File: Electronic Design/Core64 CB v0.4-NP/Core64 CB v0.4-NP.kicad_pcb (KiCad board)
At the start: 2 copper layers, 85 x 85 mm, 16 parts, among them J1 TSM-116-03-T-SV‎, J2 TSM-116-03-T-SV‎, U1 SI7210-B-01, U2 SI7210-B-02, U3 SI7210-B-03, U4 SI7210-B-04, U5 LTR-329ALS-01, X1 SAO_conn_SFH11-NBPC-D03-ST-BK

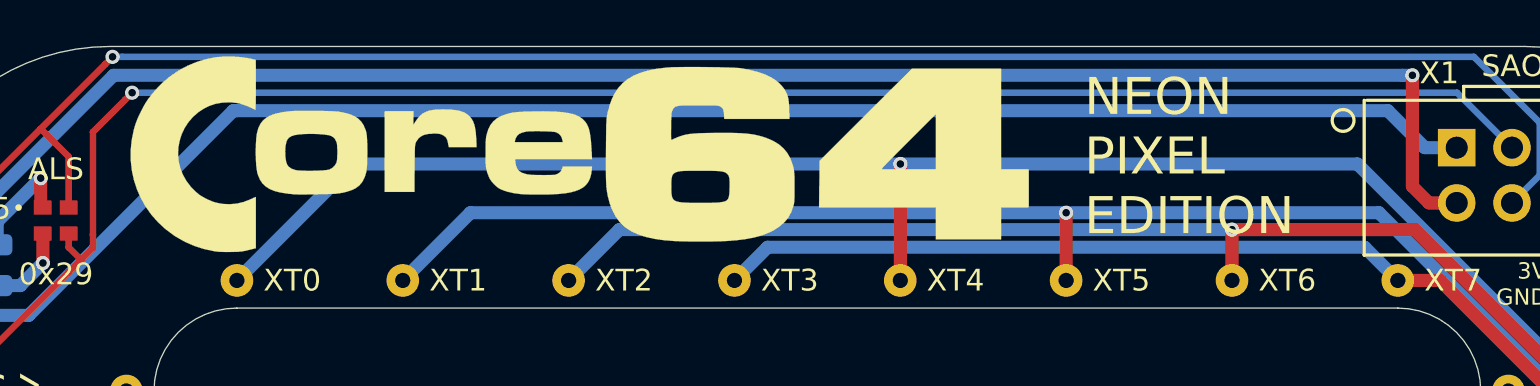
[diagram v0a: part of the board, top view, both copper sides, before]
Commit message: Tweak LB V0.4-NP Core64 logo position
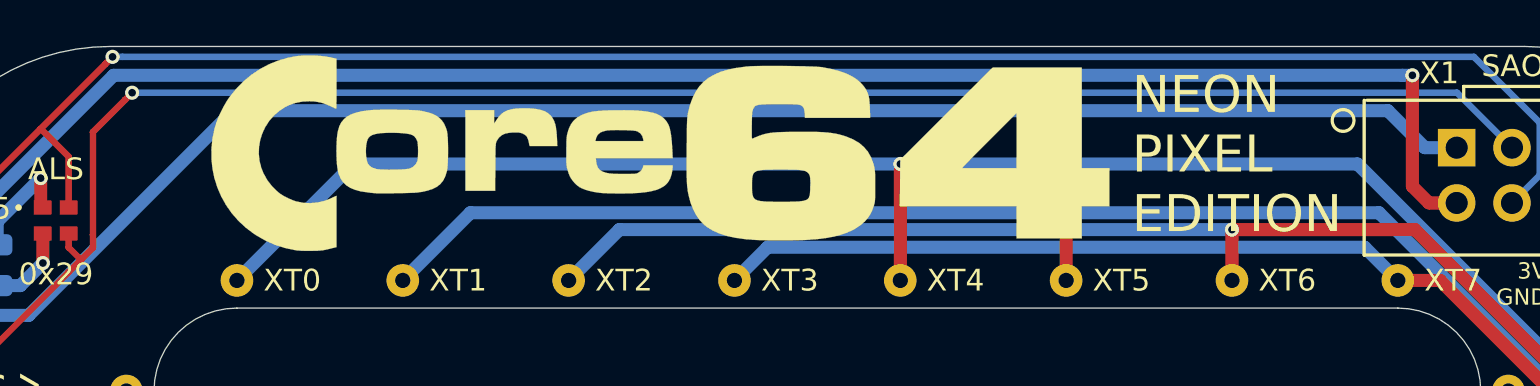
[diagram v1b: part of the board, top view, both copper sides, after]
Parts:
- moved L1 3.71 mm to (-5.33, -37.6)
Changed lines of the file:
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@@
   )
   (module Core_Memory_8x8_Array:Core64_Logo_9mm_tall (layer F.Cu)
-    (at -9.035 -37.57)
+    (at -5.3266 -37.6208)
     (fp_text reference L1 (at 0 -27) (layer F.SilkS) hide
       (effects (font (size 1.524 1.524) (thickness 0.3)))
@@
   (gr_line (start 30.48 -26.67) (end 30.48 26.67) (layer Edge.Cuts) (width 0.05))
   (gr_line (start -26.67 -30.48) (end 26.67 -30.48) (layer Edge.Cuts) (width 0.05))
-  (gr_text "NEON\nPIXEL\nEDITION" (at 12.265 -37.45) (layer F.SilkS)
+  (gr_text "NEON\nPIXEL\nEDITION" (at 14.4526 -37.5412) (layer F.SilkS)
     (effects (font (size 1.7 1.7) (thickness 0.4)) (justify left))
   )

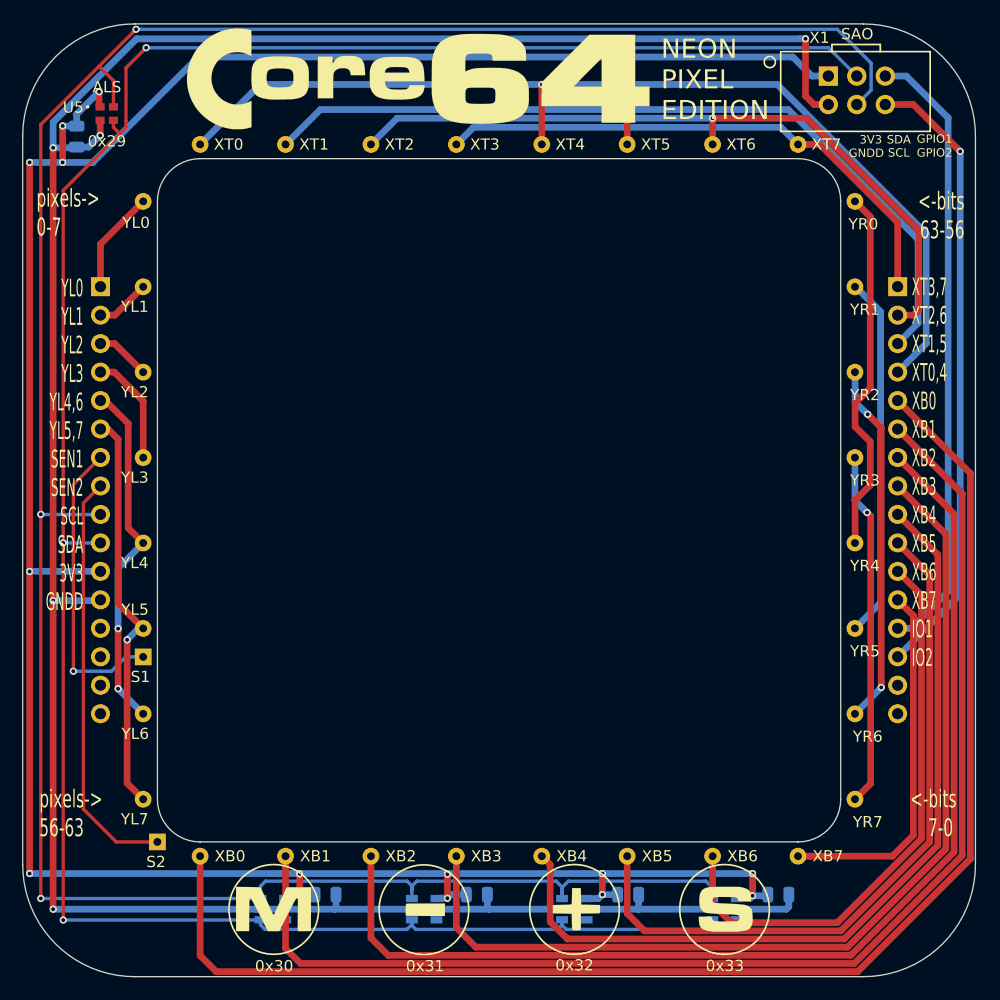
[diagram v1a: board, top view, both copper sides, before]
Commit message: Complete layout and create NP Gerbers for quote
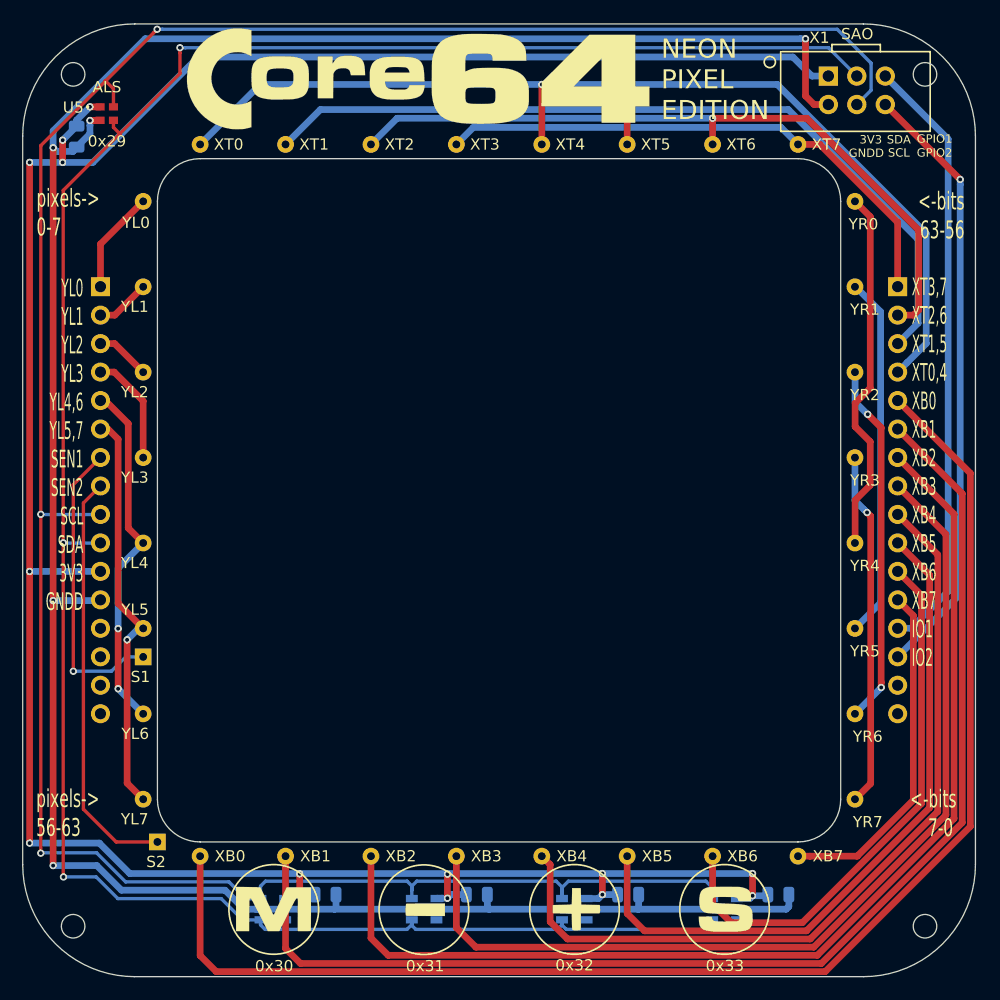
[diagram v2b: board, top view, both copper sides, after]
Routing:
- net I2C_CLOCK: track 228.4 -> 223.4 mm
- net 3V3_800mA: track 239.4 -> 234.9 mm
- net I2C_DATA: track 212.5 -> 208.4 mm
- net GNDD: track 228.8 -> 226.3 mm
- net XB7: track 32.6 -> 30.8 mm
- net XB6: track 51.4 -> 49.6 mm
- net XB5: track 63.9 -> 62.1 mm
- net XB4: track 75.8 -> 74.1 mm
- net XB3: track 88.6 -> 86.8 mm
- net XB2: track 101.1 -> 99.3 mm
- net XB1: track 113.7 -> 111.9 mm
- net XB0: track 125.9 -> 124.2 mm
- net SAO_GPIO2: track 55.8 -> 54.4 mm
- net SAO_GPIO1: track 55.3 -> 54.2 mm
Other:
- outline, holes or cut-outs redrawn
- board text added: "CORE BOARD V0.4-NP NEON PIXELS EDITION 2020-11-24 ANDY GEPPERT"
- board text removed: "CORE BOARD V0.4-NP NEON PIXELS EDITION 2020-11-23 ANDY GEPPERT"

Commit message: Update Simple Add Ons #2 on all schematics PCBs
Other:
- board text added: "J1"
- board text added: "J2"
- board text added: "NEON PIXELS BY PIERRE MUTH PIERREMUTH.WORDPRESS.COM"
- board text added: "SAO#2"
- board text added: "X1"
- board text removed: "BY PIERRE MUTH PIERREMUTH.WORDPRESS.COM"
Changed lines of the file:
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@@
   (general
     (thickness 1.6)
-    (drawings 55)
+    (drawings 59)
     (tracks 366)
     (zones 0)
@@
     (descr "Through hole straight IDC box header, 2x03, 2.54mm pitch, double rows")
     (tags "Through hole IDC box header THT 2x03 2.54mm double row")
-    (fp_text reference X1 (at -3.28 -4.675) (layer F.SilkS)
+    (fp_text reference X1 (at -3.24 -4.55) (layer F.SilkS)
       (effects (font (size 1 1) (thickness 0.15)))
     )
@@
       (effects (font (size 1 1) (thickness 0.15)))
     )
-    (fp_text user SAO (at 0.1 -5) (layer F.SilkS)
+    (fp_text user SAO#2 (at 0.1 -5) (layer F.SilkS)
       (effects (font (size 1 1) (thickness 0.15)))
     )
@@
       (effects (font (size 0.75 0.75) (thickness 0.15)) (justify mirror))
     )
-    (fp_text user GPIO2 (at 3.2 3.048) (layer B.SilkS)
+    (fp_text user GPIO2 (at 3.4 3.048) (layer B.SilkS)
       (effects (font (size 0.75 0.75) (thickness 0.15)) (justify mirror))
     )
-    (fp_text user SCL (at 0 3.048) (layer B.SilkS)
+    (fp_text user SCL (at 0.2 3.048) (layer B.SilkS)
       (effects (font (size 0.75 0.75) (thickness 0.15)) (justify mirror))
     )
@@
       (effects (font (size 0.75 0.75) (thickness 0.15)) (justify mirror))
     )
-    (fp_text user GNDD (at -3 3.048) (layer B.SilkS)
+    (fp_text user GNDD (at -2.8 3.048) (layer B.SilkS)
       (effects (font (size 0.75 0.75) (thickness 0.15)) (justify mirror))
     )
@@
     )
   )
+  (gr_text SAO#2 (at 38.415 -35.45) (layer B.SilkS)
+    (effects (font (size 1 1) (thickness 0.15)) (justify mirror))
+  )
+  (gr_text J2 (at 35.615 -21.35) (layer F.SilkS)
+    (effects (font (size 1 1) (thickness 0.16)))
+  )
+  (gr_text J1 (at -35.485 -21.35) (layer F.SilkS)
+    (effects (font (size 1 1) (thickness 0.16)))
+  )
+  (gr_text X1 (at 27.015 -37.75) (layer B.SilkS)
+    (effects (font (size 1 1) (thickness 0.15)) (justify mirror))
+  )
   (dimension 76 (width 0.15) (layer Dwgs.User)
     (gr_text "76.000 mm" (at 56.915 0 270) (layer Dwgs.User)
@@
   (gr_circle (center -6.7056 36.5252) (end -2.7056 36.5252) (layer F.SilkS) (width 0.15))
   (gr_circle (center -20.1 36.5) (end -16.1 36.5) (layer F.SilkS) (width 0.15))
-  (gr_text "BY PIERRE MUTH\nPIERREMUTH.WORDPRESS.COM" (at -12.573 -34.036) (layer B.SilkS)
+  (gr_text "NEON PIXELS BY PIERRE MUTH\nPIERREMUTH.WORDPRESS.COM" (at -12.585 -34.15) (layer B.SilkS)
     (effects (font (size 1 1) (thickness 0.15)) (justify left mirror))
   )

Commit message: Export Gerbers and order 10, export updated schematic and front/back renders
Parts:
- added ?: , , F.Cu at (16.3, -8.15)
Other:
- board text added: "CORE BOARD V0.4-NP NEON PIXEL EDITION 2020-11-25 ANDY GEPPERT"
- board text removed: "CORE BOARD V0.4-NP NEON PIXELS EDITION 2020-11-24 ANDY GEPPERT"
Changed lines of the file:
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@@
     (tracks 366)
     (zones 0)
-    (modules 16)
+    (modules 17)
     (nets 41)
   )
@@
     (38 B.Mask user)
     (39 F.Mask user)
-    (40 Dwgs.User user)
+    (40 Dwgs.User user hide)
     (41 Cmts.User user hide)
     (42 Eco1.User user hide)
@@
       (drillshape 0)
       (scaleselection 1)
-      (outputdirectory "Core64 CB v0.4-NP Gerbers (2020-11-24)/"))
+      (outputdirectory "Core64 CB v0.4-NP Gerbers (2020-11-25)/"))
   )
   (net 0 "")
@@
     (add_net SENSE2)
   )
+  (module "" (layer F.Cu)
+    (at 16.315 -8.15)
+    (fp_text reference "" (at 31.855 -36.6) (layer F.SilkS)
+      (effects (font (size 1.27 1.27) (thickness 0.15)))
+    )
+    (fp_text value "" (at 31.855 -36.6) (layer F.SilkS)
+      (effects (font (size 1.27 1.27) (thickness 0.15)))
+    )
+    (fp_text user GPIO1 (at 24.2 -24) (layer F.SilkS)
+      (effects (font (size 0.75 0.75) (thickness 0.15)))
+    )
+    (fp_text user GPIO2 (at 24.2 -22.8) (layer F.SilkS)
+      (effects (font (size 0.75 0.75) (thickness 0.15)))
+    )
+    (fp_text user SCL (at 20.9 -22.8) (layer F.SilkS)
+      (effects (font (size 0.75 0.75) (thickness 0.15)))
+    )
+    (fp_text user GNDD (at 17.7 -22.8) (layer F.SilkS)
+      (effects (font (size 0.75 0.75) (thickness 0.15)))
+    )
+    (fp_text user 3V3 (at 17.7 -24) (layer F.SilkS)
+      (effects (font (size 0.75 0.75) (thickness 0.15)))
+    )
+    (fp_text user SDA (at 20.8 -24) (layer F.SilkS)
+      (effects (font (size 0.75 0.75) (thickness 0.15)))
+    )
+  )
   (module badgelife_sao_v169bis:Badgelife-SAOv169-BADGE-2x3 (layer F.Cu)
     (at 31.855 -36.6)
@@
       (effects (font (size 1 1) (thickness 0.15)))
     )
+    (fp_line (start 6.604 3.683) (end 6.604 2.754) (layer F.SilkS) (width 0.15))
+    (fp_line (start 6.604 -2.5) (end 6.604 -3.429) (layer F.SilkS) (width 0.15))
+    (fp_line (start 6.604 -3.429) (end 5.873 -3.429) (layer F.SilkS) (width 0.15))
+    (fp_line (start 6.604 3.683) (end 5.873 3.683) (layer F.SilkS) (width 0.15))
+    (fp_line (start -6.731 3.683) (end -6.731 2.754) (layer F.SilkS) (width 0.15))
+    (fp_line (start -6.731 -3.429) (end -6 -3.429) (layer F.SilkS) (width 0.15))
     (fp_text user SAO#2 (at 0.1 -5) (layer F.SilkS)
       (effects (font (size 1 1) (thickness 0.15)))
-    )
-    (fp_text user 3V3 (at 1.31 4.419) (layer F.SilkS)
-      (effects (font (size 0.75 0.75) (thickness 0.15)))
-    )
-    (fp_text user GNDD (at 0.91 5.619) (layer F.SilkS)
-      (effects (font (size 0.75 0.75) (thickness 0.15)))
-    )
-    (fp_text user SDA (at 3.81 4.419) (layer F.SilkS)
-      (effects (font (size 0.75 0.75) (thickness 0.15)))
-    )
-    (fp_text user SCL (at 3.81 5.592) (layer F.SilkS)
-      (effects (font (size 0.75 0.75) (thickness 0.15)))
-    )
-    (fp_text user GPIO2 (at 6.997 5.592) (layer F.SilkS)
-      (effects (font (size 0.75 0.75) (thickness 0.15)))
-    )
-    (fp_text user GPIO1 (at 6.997 4.35) (layer F.SilkS)
-      (effects (font (size 0.75 0.75) (thickness 0.15)))
     )
     (fp_text user GPIO1 (at 3.2 -2.794) (layer B.SilkS)
       (effects (font (size 0.75 0.75) (thickness 0.15)) (justify mirror))
     )
-    (fp_text user GPIO2 (at 3.4 3.048) (layer B.SilkS)
+    (fp_text user GPIO2 (at 3.2 3.048) (layer B.SilkS)
       (effects (font (size 0.75 0.75) (thickness 0.15)) (justify mirror))
     )
-    (fp_text user SCL (at 0.2 3.048) (layer B.SilkS)
+    (fp_text user SCL (at 0 3.048) (layer B.SilkS)
       (effects (font (size 0.75 0.75) (thickness 0.15)) (justify mirror))
     )
@@
       (effects (font (size 0.75 0.75) (thickness 0.15)) (justify mirror))
     )
-    (fp_text user GNDD (at -2.8 3.048) (layer B.SilkS)
+    (fp_text user GNDD (at -3 3.048) (layer B.SilkS)
       (effects (font (size 0.75 0.75) (thickness 0.15)) (justify mirror))
     )
@@
     (fp_line (start 2.159 -4.064) (end 2.159 -3.43) (layer F.SilkS) (width 0.15))
     (fp_line (start -2.159 -4.064) (end 2.159 -4.064) (layer F.SilkS) (width 0.15))
-    (fp_line (start -6.731 3.683) (end -6.731 -3.429) (layer F.SilkS) (width 0.15))
-    (fp_line (start 6.604 3.683) (end -6.731 3.683) (layer F.SilkS) (width 0.15))
-    (fp_line (start 6.604 -3.429) (end 6.604 3.683) (layer F.SilkS) (width 0.15))
-    (fp_line (start -6.604 -3.429) (end 6.604 -3.429) (layer F.SilkS) (width 0.15))
+    (fp_line (start -6.731 -2.5) (end -6.731 -3.429) (layer F.SilkS) (width 0.15))
+    (fp_line (start -6 3.683) (end -6.731 3.683) (layer F.SilkS) (width 0.15))
     (fp_text user %R (at 0.06 0.02 270) (layer F.Fab)
+      (effects (font (size 1 1) (thickness 0.15)))
+    )
+    (fp_text user SAO#2 (at 0.1 -5) (layer F.SilkS)
       (effects (font (size 1 1) (thickness 0.15)))
     )
@@
     (arrow2b (pts (xy 42.5 -50.549999) (xy 41.373496 -49.963578)))
   )
-  (gr_text "CORE BOARD   V0.4-NP   NEON PIXELS EDITION   2020-11-24   ANDY GEPPERT   " (at -0.685 -41.35) (layer B.SilkS)
+  (gr_text "CORE BOARD   V0.4-NP   NEON PIXEL EDITION   2020-11-25   ANDY GEPPERT   " (at 0 -41.5) (layer B.SilkS)
     (effects (font (size 1 1) (thickness 0.15)) (justify mirror))
   )
@@
   (gr_arc (start -32.5 32.5) (end -32.5 42.5) (angle 90) (layer Edge.Cuts) (width 0.05))
   (gr_line (start -32.5 42.5) (end 32.5 42.5) (layer Edge.Cuts) (width 0.05))
-  (gr_text "Interactive Core Memory\nand Neon Pixels!" (at 24.765 -36.322) (layer B.SilkS)
+  (gr_text "Interactive Core Memory\nand Neon Pixels!" (at 24.765 -36.5) (layer B.SilkS)
     (effects (font (size 2.7 2.7) (thickness 0.5)) (justify left mirror))
   )
